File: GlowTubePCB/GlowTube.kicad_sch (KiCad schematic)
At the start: 25 parts, among them Q1 MMBT2222A, Q2 MMBT2222A, U1 ESP32-WROOM-32E (4MB), U2 SN74AHCT32QPWRQ1, U3 BL1117-33CX, U4 CP2102-GMR

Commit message: added GlowTube v1.0 beta 1
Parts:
- added C10: 1uF, Capacitor_SMD:C_0603_1608Metric_Pad1.08x0.95mm_HandSolder, symbol Device:1uF 0603
- added J1: Conn_01x08, Connector_PinSocket_2.54mm:PinSocket_1x08_P2.54mm_Vertical, symbol Connector_Generic:Conn_01x08
- added LED2: LED_strip_contact_pads, Connector:LED strip connector pad, symbol Connector:LED_strip_contact_pads
- added Q3, Q4: AP40P05, Package_TO_SOT_SMD:SOT-23, symbol Transistor_FET:SK338P
- added R7: 10K, Resistor_SMD:R_0603_1608Metric_Pad0.98x0.95mm_HandSolder, symbol Device:10K 0603
- added RJ1: R-RJ11R06P-A800, R-RJ11R06P-A800:R-RJ11R06P-A800, symbol R-RJ11R06P-A800:PCB-6P6C-90
- added SW1, SW2: TS-1185EC-C-D-B, TS-1185EC-C-D-B:TS-1185EC-C-D-B, symbol TS-1185EC-C-D-B:TS-1185EC-C-D-B
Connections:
- net USB-C 5V is gone; now on net +5V: C3.2, F1.2, U3.3 (Vin), U4.8 (VBUS)
- net +3V3: now also J1.6 (Pin_6), Q4.3 (D), R7.2; no longer C7.2, U3.2 (Vout), U3.4 (Vout)
- net +5V: now also J1.8 (Pin_8), LED2.1 (5V)
- net GND: now also C10.1, J1.7 (Pin_7), LED2.3 (GND), RJ1.4, SW1.1, SW2.1
- net IO12: now also J1.1 (Pin_1)
- net IO13: now also J1.2 (Pin_2)
- net IO16/LED1: now also Q3.2 (S); no longer U2.1 (1A)
- net IO25/A1/DAC1: now also J1.4 (Pin_4)
- net IO26/A0/DAC2: now also J1.5 (Pin_5)
- net IO5: now also J1.3 (Pin_3)
- net RESET: now also C10.2, R7.1, SW2.2
- net IO33 renamed IO33/TESTBUTTON
- net IO33/TESTBUTTON: now also SW1.2
- new net: C7.2, Q4.2 (S), U3.2 (Vout), U3.4 (Vout)
- new net LED1 DATA IN: Q3.3 (D), RJ1.3, U2.1 (1A)
- new net RECEIVER 5V: Q3.1 (G), Q4.1 (G), RJ1.2
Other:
- note added: "Pins"
- note added: "Receiver mode"
- note added: "Reset"
- note added: "Test animations button"
- note removed: "Pins/Pads"
- moved on the sheet: C3, C4, C5, C6, C7, C8, F1, LED1, MK1, Q1, Q2, R2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

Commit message: updated pcb design
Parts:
- removed C10: 1uF, Capacitor_SMD:C_0603_1608Metric_Pad1.08x0.95mm_HandSolder, symbol Device:1uF 0603
- removed C5: 10uF, Capacitor_SMD:C_0603_1608Metric_Pad1.08x0.95mm_HandSolder, symbol Device:10uF 0603
- removed C8: 0.1uF, Capacitor_SMD:C_0603_1608Metric_Pad1.08x0.95mm_HandSolder, symbol Device:0.1uF 0603
- removed MK1: ICS-43432, ICS-43432:MIC_ICS-43432, symbol ICS-43432:ICS-43432
- removed Q1, Q2: MMBT2222A, Package_TO_SOT_SMD:SOT-23, symbol MMBT2222A:MMBT2222A
- removed Q4: AP40P05, Package_TO_SOT_SMD:SOT-23, symbol Transistor_FET:SK338P
- removed R4, R5, R7: 10K, Resistor_SMD:R_0603_1608Metric_Pad0.98x0.95mm_HandSolder, symbol Device:10K 0603
- removed R6: 100K, Resistor_SMD:R_0603_1608Metric_Pad0.98x0.95mm_HandSolder, symbol Device:100K 0603
- removed SW2: TS-1185EC-C-D-B, TS-1185EC-C-D-B:TS-1185EC-C-D-B, symbol TS-1185EC-C-D-B:TS-1185EC-C-D-B
- added C11: 0.1uF, Capacitor_SMD:C_0603_1608Metric_Pad1.08x0.95mm_HandSolder, symbol Device:0.1uF 0603
- added C? (x2): 1nF, Capacitor_SMD:C_0603_1608Metric_Pad1.08x0.95mm_HandSolder, symbol Device:10uF 0603
- added C?: 10uF, Capacitor_SMD:C_0603_1608Metric_Pad1.08x0.95mm_HandSolder, symbol Device:10uF 0603
- added R? (x2): 220, Resistor_SMD:R_0603_1608Metric_Pad0.98x0.95mm_HandSolder, symbol Device:10K 0603
- added R? (x3): 10K, Resistor_SMD:R_0603_1608Metric_Pad0.98x0.95mm_HandSolder, symbol Device:10K 0603
- added R?: 1K, Resistor_SMD:R_0603_1608Metric_Pad0.98x0.95mm_HandSolder, symbol Device:10K 0603
- added SW? (x2): TS-1185EC-C-D-B, TS-1185EC-C-D-B:TS-1185EC-C-D-B, symbol TS-1185EC-C-D-B:TS-1185EC-C-D-B
- added U6: GMA4030H11-F26, GMA4030H11-F26:GMA4030H11-F26, symbol GMA4030H11-F26:GMA4030H11-F26
- added U?: UMH3N, footprint:SC-70-6_L2.2-W1.3-P0.65-LS2.1-BR, symbol LCSC:UMH3N
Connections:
- net +3V3: now also C7.2, U3.2 (Vout), U3.4 (Vout), C11.2, C?.2, R?.2, R?.2, U6.1 (VDD)
- net DTR: now also U?.2 (B), U?.4 (E)
- net GND: now also C11.1, C?.1, C?.2, C?.2, SW?.1, SW?.1, U6.5 (GND), U6.6 (GND), U6.7 (GND), U6.8 (GND)
- net IO0: now also C?.1, R?.1, R?.2, U?.3 (C)
- net IO14/SCK: now also U6.3 (CLOCK)
- net IO15/WS: now also U6.2 (SELECT)
- net IO32/SD: now also U6.4 (DATA)
- net RECEIVER 5V: no longer Q3.1 (G)
- net RESET: now also C?.1, R?.1, R?.2, U?.6 (C)
- net RTS: now also U?.1 (E), U?.5 (B)
- new net: R?.1, SW?.2 (x2)
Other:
- note added: "Auto program DTR RTS --> EN IO0 1 1 1 1 0 0 1 1 1 0 0 1 0 1 1 0"
- moved on the sheet: C3, C7, Q3, R2, R3, U3

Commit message: redesigned GlowTube PCBs
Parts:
- removed C1, C9: 220uF 10V, Capacitor_SMD:CP_Elec_6.3x5.4, symbol Device:C_Polarized
- removed C11: 0.1uF, Capacitor_SMD:C_0603_1608Metric_Pad1.08x0.95mm_HandSolder, symbol Device:0.1uF 0603
- removed C3, C?: 10uF, Capacitor_SMD:C_0603_1608Metric_Pad1.08x0.95mm_HandSolder, symbol Device:10uF 0603
- removed C4: 4.7uF 6.3V 10%, Capacitor_SMD:C_0603_1608Metric_Pad1.08x0.95mm_HandSolder, symbol Device:C
- removed C? (x2): 1nF, Capacitor_SMD:C_0603_1608Metric_Pad1.08x0.95mm_HandSolder, symbol Device:10uF 0603
- removed J1: Conn_01x08, Connector_PinSocket_2.54mm:PinSocket_1x08_P2.54mm_Vertical, symbol Connector_Generic:Conn_01x08
- removed LED1, LED2: LED_strip_contact_pads, Connector:LED strip connector pad, symbol Connector:LED_strip_contact_pads
- removed Q3: AP40P05, Package_TO_SOT_SMD:SOT-23, symbol Transistor_FET:SK338P
- removed R? (x2): 220, Resistor_SMD:R_0603_1608Metric_Pad0.98x0.95mm_HandSolder, symbol Device:10K 0603
- removed R? (x3): 10K, Resistor_SMD:R_0603_1608Metric_Pad0.98x0.95mm_HandSolder, symbol Device:10K 0603
- removed R?: 1K, Resistor_SMD:R_0603_1608Metric_Pad0.98x0.95mm_HandSolder, symbol Device:10K 0603
- removed RJ1: R-RJ11R06P-A800, R-RJ11R06P-A800:R-RJ11R06P-A800, symbol R-RJ11R06P-A800:PCB-6P6C-90
- removed SW? (x2): TS-1185EC-C-D-B, TS-1185EC-C-D-B:TS-1185EC-C-D-B, symbol TS-1185EC-C-D-B:TS-1185EC-C-D-B
- removed U1: ESP32-WROOM-32E (4MB), ESP32-WROOM-32E__16MB_:MODULE_ESP32-WROOM-32E_(16MB), symbol ESP32-WROOM-32E__16MB_:ESP32-WROOM-32E (4MB)
- removed U2: SN74AHCT32QPWRQ1, SN74AHCT32QPWRQ1:SN74AHCT32QPWRQ1, symbol SN74AHCT32QPWRQ1:SN74AHCT32QPWRQ1
- removed U3: BL1117-33CX, Package_TO_SOT_SMD:SOT-223, symbol BL1117-33CX:BL1117-33CX
- removed U4: CP2102-GMR, CP2102-GMR:CP2102-GMR, symbol CP2102-GMR:CP2102-GMR
- removed U?: UMH3N, footprint:SC-70-6_L2.2-W1.3-P0.65-LS2.1-BR, symbol LCSC:UMH3N
- added C1, C8: 10uF, Capacitor_SMD:C_0603_1608Metric_Pad1.08x0.95mm_HandSolder, symbol Device:10uF 0603
- added C10, C11: 1nF, Capacitor_SMD:C_0603_1608Metric_Pad1.08x0.95mm_HandSolder, symbol Device:10uF 0603
- added C12: KAN0637-0701B, footprint:SW-TH_KAN0637-0701B, symbol LCSC:KAN0637-0701B
- added C3, C4: 220uF 10V, Capacitor_SMD:CP_Elec_6.3x5.4, symbol Device:220uF 10V 6.3x5.4mm
- added C5: 4.7uF 6.3V 10%, Capacitor_SMD:C_0603_1608Metric_Pad1.08x0.95mm_HandSolder, symbol Device:C
- added C9: 0.1uF, Capacitor_SMD:C_0603_1608Metric_Pad1.08x0.95mm_HandSolder, symbol Device:0.1uF 0603
- added J1: Conn_01x07, Connector_PinSocket_2.54mm:PinSocket_1x07_P2.54mm_Vertical, symbol Connector_Generic:Conn_01x07
- added P1, P2, P3, P4, P5, P6: Solder_Pad, footprint:Solder pad, symbol LCSC:Solder_Pad
- added R4, R5: 220, Resistor_SMD:R_0603_1608Metric_Pad0.98x0.95mm_HandSolder, symbol Device:10K 0603
- added R6, R7: 10K, Resistor_SMD:R_0603_1608Metric_Pad0.98x0.95mm_HandSolder, symbol Device:10K 0603
- added R8: 62, Resistor_SMD:R_0603_1608Metric_Pad0.98x0.95mm_HandSolder, symbol Device:R
- added SW2: TS-1185EC-C-D-B, TS-1185EC-C-D-B:TS-1185EC-C-D-B, symbol TS-1185EC-C-D-B:TS-1185EC-C-D-B
- added U1: SN74AHCT32QPWRQ1, SN74AHCT32QPWRQ1:SN74AHCT32QPWRQ1, symbol SN74AHCT32QPWRQ1:SN74AHCT32QPWRQ1
- added U2: ESP32-WROOM-32E (4MB), ESP32-WROOM-32E__16MB_:MODULE_ESP32-WROOM-32E_(16MB), symbol ESP32-WROOM-32E__16MB_:ESP32-WROOM-32E (4MB)
- added U3: CP2102-GMR, CP2102-GMR:CP2102-GMR, symbol CP2102-GMR:CP2102-GMR
- added U4: BL1117-33CX, Package_TO_SOT_SMD:SOT-223, symbol BL1117-33CX:BL1117-33CX
- added U5: UMH3N, footprint:SC-70-6_L2.2-W1.3-P0.65-LS2.1-BR, symbol LCSC:UMH3N
- C2: LCSC # (none) -> C14663
- C6: 1500+ €0.0119 -> (none); 50+ €0.0171 -> (none); 500+ €0.0141 -> (none); LCSC Part # C597194 -> C14663; LCSC link https://lcsc.com/product-detail/Multilayer-Ceramic-Capacito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 -> (none); Manufacturer AVX -> (none); Mfr. Part #  06035C104K4Z2A -> (none); Package 0603 -> (none)
- C7: 10+ €0.0665 -> (none); 100+ €0.0537 -> (none); 20+ €0.0301 -> (none); 200+ €0.0246 -> (none); 300+ €0.0445 -> (none); 600+ €0.0208 -> (none); LCSC Part # C729457 -> C19702; LCSC link https://lcsc.com/product-detail/Multilayer-Ceramic-Capacito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 -> (none); Manufacturer SANYEAR -> (none); Mfr. Part # C0603X5R106K250NT -> (none); Package 0603 -> (none)
- F1: LCSC # (none) -> C883162
- R1: LCSC # (none) -> C177352
- R2, R3: 50+ € 0.0090 -> (none); 500+ € 0.0075 -> (none); LCSC Part # C365193 -> C23186; LCSC link https://lcsc.com/product-detail/Chip-Resistor-Surface-Mount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 -> (none); Manufacturer Resistor.Today -> (none); Mfr. Part # HPCR0603F5K10K9 -> (none); Package 0603 -> (none)
- U6: LCSC # (none) -> C498193
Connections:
- net +3V3: now also C1.2, C5.2, C8.2, C9.2, J1.5 (Pin_5), R6.2, R7.2, U2.2 (3V3), U3.6 (VDD), U3.7 (REGIN), U4.2 (Vout), U4.4 (Vout); no longer C7.2
- net +5V: now also C7.2, C3.1, C4.1, J1.6 (Pin_6), P1.1, P4.1, U1.14 (VCC), U3.8 (VBUS), U4.3 (Vin)
- net DTR: now also U3.28 (DTR), U5.2 (B), U5.4 (E)
- net GND: now also C1.1, C10.2, C11.2, C12.1, C3.2, C4.2, C5.1, C8.1, C9.1, J1.7 (Pin_7), P3.1, P5.1, SW2.1, U1.10 (3B), U1.11 (4Y), U1.12 (4A), U1.13 (4B), U1.2 (1B), U1.5 (2B), U1.7 (GND), U1.8 (3Y), U1.9 (3A), U2.1 (GND), U2.15 (GND), U2.38 (GND), U2.39_1 (GND), U2.39_10 (GND), U2.39_11 (GND), U2.39_12 (GND), U2.39_13 (GND), U2.39_14 (GND), U2.39_15 (GND), U2.39_16 (GND), U2.39_17 (GND), U2.39_18 (GND), U2.39_19 (GND), U2.39_2 (GND), U2.39_20 (GND), U2.39_21 (GND), U2.39_3 (GND), U2.39_4 (GND), U2.39_5 (GND), U2.39_6 (GND), U2.39_7 (GND), U2.39_8 (GND), U2.39_9 (GND), U3.29 (GND_PAD), U3.3 (GND), U4.1 (GND)
- net I34/A2: now also U2.6 (IO34)
- net I39/A3/SENSOR_VN: now also U2.5 (SENSOR_VN)
- net IO0: now also C11.1, R5.2, R7.1, U2.25 (IO0), U5.3 (C)
- net IO14/SCK: now also U2.13 (IO14)
- net IO15/WS: now also U2.23 (IO15)
- net IO16/LED1: now also U1.1 (1A), U2.27 (IO16)
- net IO2: now also U2.24 (IO2)
- net IO21: now also U2.33 (IO21)
- net IO22: now also U2.36 (IO22)
- net IO23: now also U2.37 (IO23)
- net IO25/A1/DAC1: now also J1.3 (Pin_3), U2.10 (IO25)
- net IO26/A0/DAC2: now also J1.4 (Pin_4), U2.11 (IO26)
- net IO27: now also U2.12 (IO27)
- net IO32/SD: now also U2.8 (IO32)
- net IO35: now also U2.7 (IO35)
- net IO36/A4/SENSOR_VP: now also U2.4 (SENSOR_VP)
- net IO4/A5: now also U2.26 (IO4)
- net IO5: now also U2.29 (IO5)
- net LED1 DATA OUT: now also P2.1
- net RESET: now also C10.1, R4.2, R6.1, U2.3 (EN), U5.6 (C)
- net RTS: now also U3.24 (RTS), U5.1 (E), U5.5 (B)
- net RXD0: now also U2.34 (RXD0), U3.26 (TXD)
- net TXD0: now also U2.35 (TXD0), U3.25 (RXD)
- net USB-C DATA+: now also U3.4 (D+)
- net USB-C DATA-: now also U3.5 (D-)
- net VBUS: now reaches F1.1, USB1.A4B9 (VBUS), USB1.B4A9 (VBUS)
- net at R1.1: now also U1.3 (1Y)
- net IO33/TESTBUTTON: no longer names the net of SW1.2
- net IO33/TESTBUTTON: now also R4.1
- new net: R8.1, U1.6 (2Y)
- new net: R5.1, SW2.2
- new net: U2.17 (NC), U2.18 (NC), U2.19 (NC), U2.20 (NC), U2.21 (NC), U2.22 (NC)
- new net IO12/MISO: J1.1 (Pin_1), U2.14 (IO12)
- new net IO13/MOSI: J1.2 (Pin_2), U2.16 (IO13)
- new net IO17/LED2: U1.4 (2A), U2.28 (IO17)
- new net IO18: U2.30 (IO18)
- new net IO19: U2.31 (IO19)
- new net IO33/MAINBUTTON: C12.2, U2.9 (IO33)
- new net LED2 DATA OUT: P6.1, R8.2
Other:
- note added: "Fuse only for GlowLight."
- note added: "Main button"
- note added: "Power & filtering"
- note removed: "Power"
- note removed: "Receiver mode"
- note removed: "Test animations button"

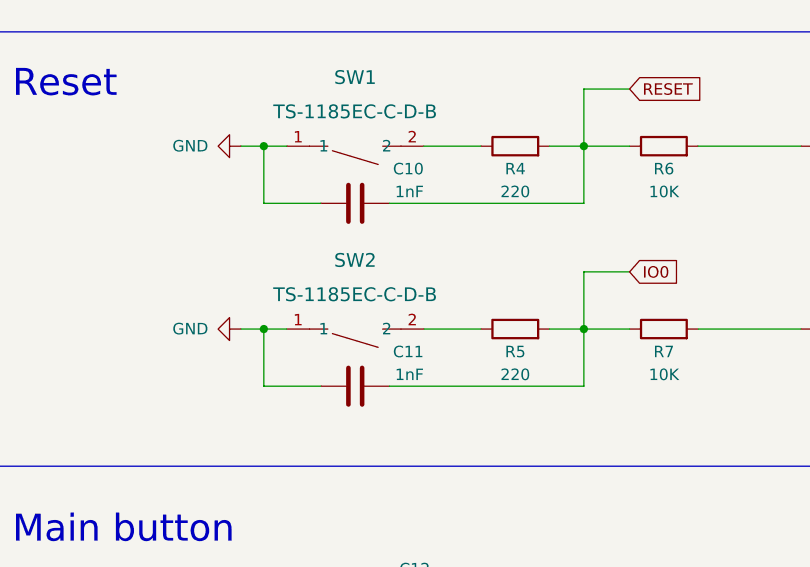
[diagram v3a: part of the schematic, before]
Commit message: updated 3d model and software upload fix
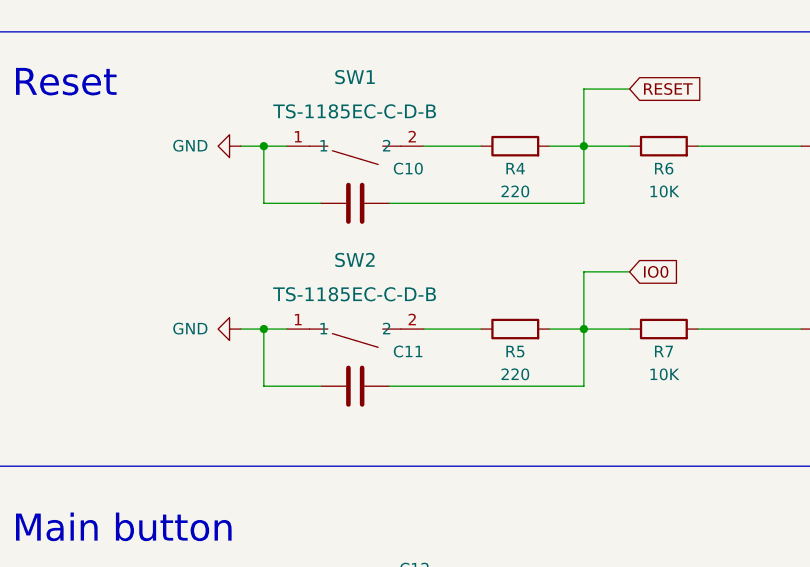
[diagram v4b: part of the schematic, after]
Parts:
- C10, C11: value 1nF -> (none)
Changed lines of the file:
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@@
       (effects (font (size 1.27 1.27)) (justify right))
     )
-    (property "Value" "1nF" (id 1) (at 349.25 209.55 90)
+    (property "Value" "" (id 1) (at 349.25 209.55 90)
       (effects (font (size 1.27 1.27)) (justify right))
     )
@@
       (effects (font (size 1.27 1.27)) (justify left) hide)
     )
-    (property "150+" "€0.0719" (id 11) (at 287.02 187.96 0)
+    (property "150+" "€0.0719" (id 12) (at 287.02 187.96 0)
       (effects (font (size 1.27 1.27)) (justify left) hide)
     )
@@
       (effects (font (size 1.27 1.27)) hide)
     )
-    (property "LCSC link" "https://lcsc.com/product-detail/span-style-background-color-ff0-USB-span-Connectors_XKB-Connectivity-U262-161N-4BVC11_C319148.html" (id 11) (at 146.05 72.39 0)
+    (property "LCSC link" "https://lcsc.com/product-detail/span-style-background-color-ff0-USB-span-Connectors_XKB-Connectivity-U262-161N-4BVC11_C319148.html" (id 12) (at 146.05 72.39 0)
       (effects (font (size 1.27 1.27)) hide)
     )
@@
       (effects (font (size 1.27 1.27)) (justify right))
     )
-    (property "Value" "1nF" (id 1) (at 349.25 189.23 90)
+    (property "Value" "" (id 1) (at 349.25 189.23 90)
       (effects (font (size 1.27 1.27)) (justify right))
     )
@@
     )
     (path "/d08fbdcd-f70c-4667-ac9a-76d0b64315e8"
-      (reference "C10") (unit 1) (value "1nF") (footprint "Capacitor_SMD:C_0603_1608Metric_Pad1.08x0.95mm_HandSolder")
+      (reference "C10") (unit 1) (value "1uF") (footprint "Capacitor_SMD:C_0603_1608Metric_Pad1.08x0.95mm_HandSolder")
     )
     (path "/01727eb1-7919-4fdf-a883-a0981fe537d4"
-      (reference "C11") (unit 1) (value "1nF") (footprint "Capacitor_SMD:C_0603_1608Metric_Pad1.08x0.95mm_HandSolder")
+      (reference "C11") (unit 1) (value "1uF") (footprint "Capacitor_SMD:C_0603_1608Metric_Pad1.08x0.95mm_HandSolder")
     )
     (path "/e3e65532-68f9-47d6-b6e3-3f0dccfcd490"

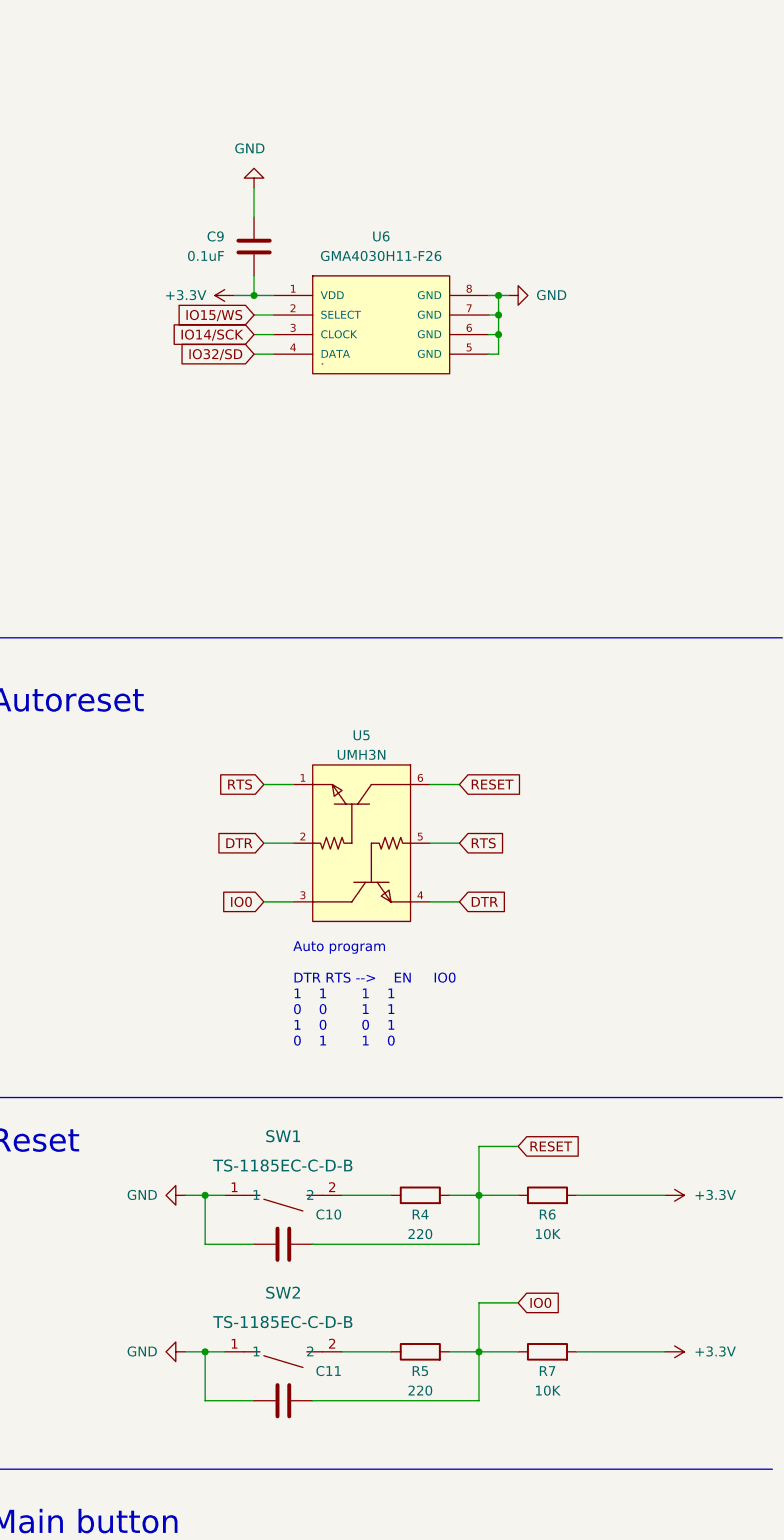
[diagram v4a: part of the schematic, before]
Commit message: added temp wall mount and updated mic
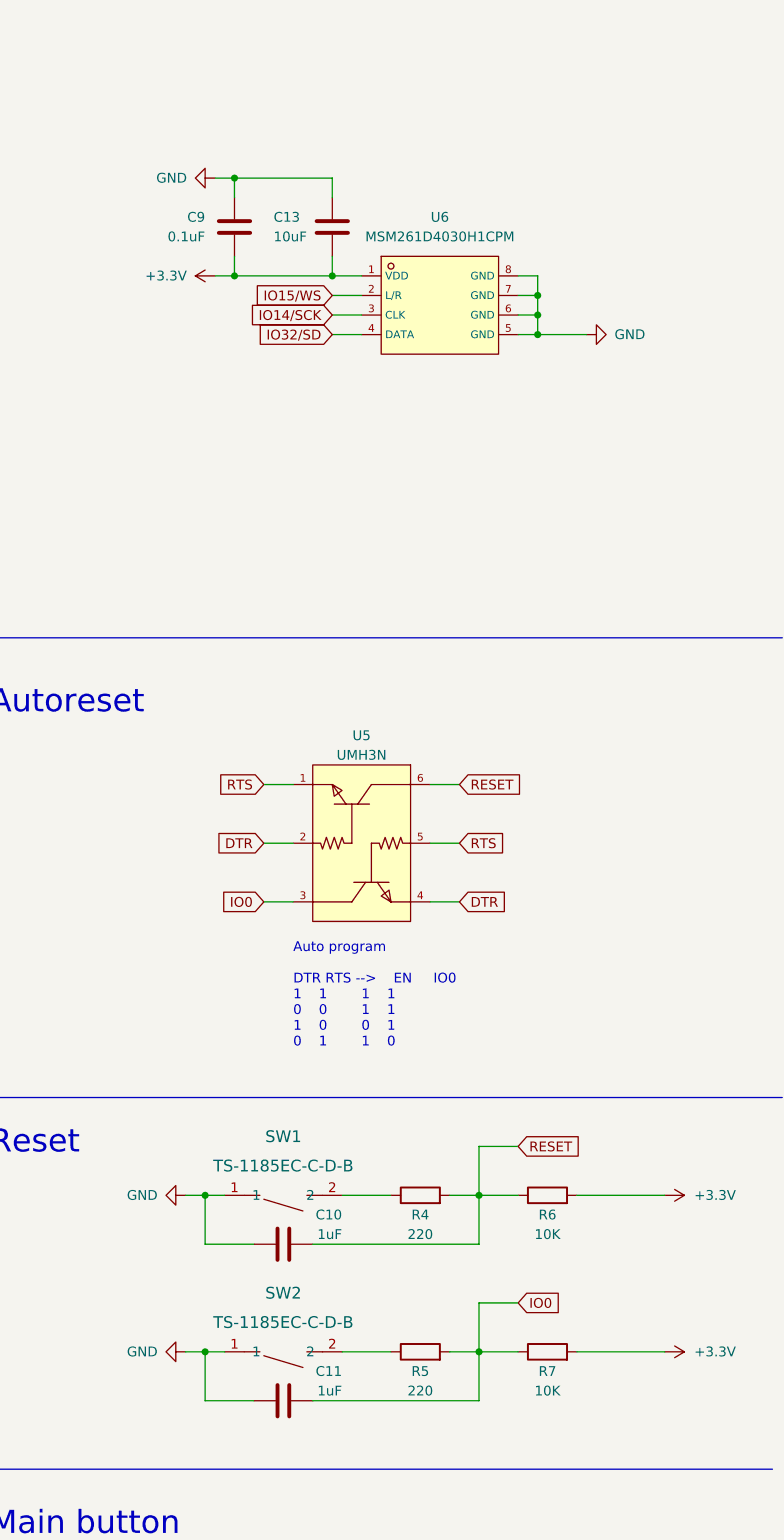
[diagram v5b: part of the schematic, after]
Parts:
- removed U6: GMA4030H11-F26, GMA4030H11-F26:GMA4030H11-F26, symbol GMA4030H11-F26:GMA4030H11-F26
- added C13: 10uF, Capacitor_SMD:C_0603_1608Metric_Pad1.08x0.95mm_HandSolder, symbol Device:0.1uF 0603
- added U6: MSM261D4030H1CPM, footprint:MIC-SMD_8P-L3.0-W4.0-P0.85-BL, symbol MyParts:MSM261D4030H1CPM
- C10, C11: value (none) -> 1uF
- C9: 1500+ (none) -> €0.0119; 50+ (none) -> €0.0171; 500+ (none) -> €0.0141; LCSC Part # C14663 -> C597194; LCSC link (none) -> https://lcsc.com/product-detail/Multilayer-Ceramic-Capacito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; Manufacturer (none) -> AVX; Mfr. Part # (none) -> 06035C104K4Z2A; Package (none) -> 0603
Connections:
- net +3V3: now also C13.2, U6.1 (VDD)
- net GND: now also C13.1, U6.5 (GND), U6.6 (GND), U6.7 (GND), U6.8 (GND)
- net IO14/SCK: now also U6.3 (CLK)
- net IO15/WS: now also U6.2 (L/R)
- net IO32/SD: now also U6.4 (DATA)
